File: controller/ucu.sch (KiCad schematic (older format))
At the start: 127 parts, among them J2 AMP_1, J24 AMP_4, J25 AMP_5, J26 AMP_6, J3 BUTTON, J4 AMP_2, J40 LCD, J41 TempSens1, J42 TempSens2, J47 USB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

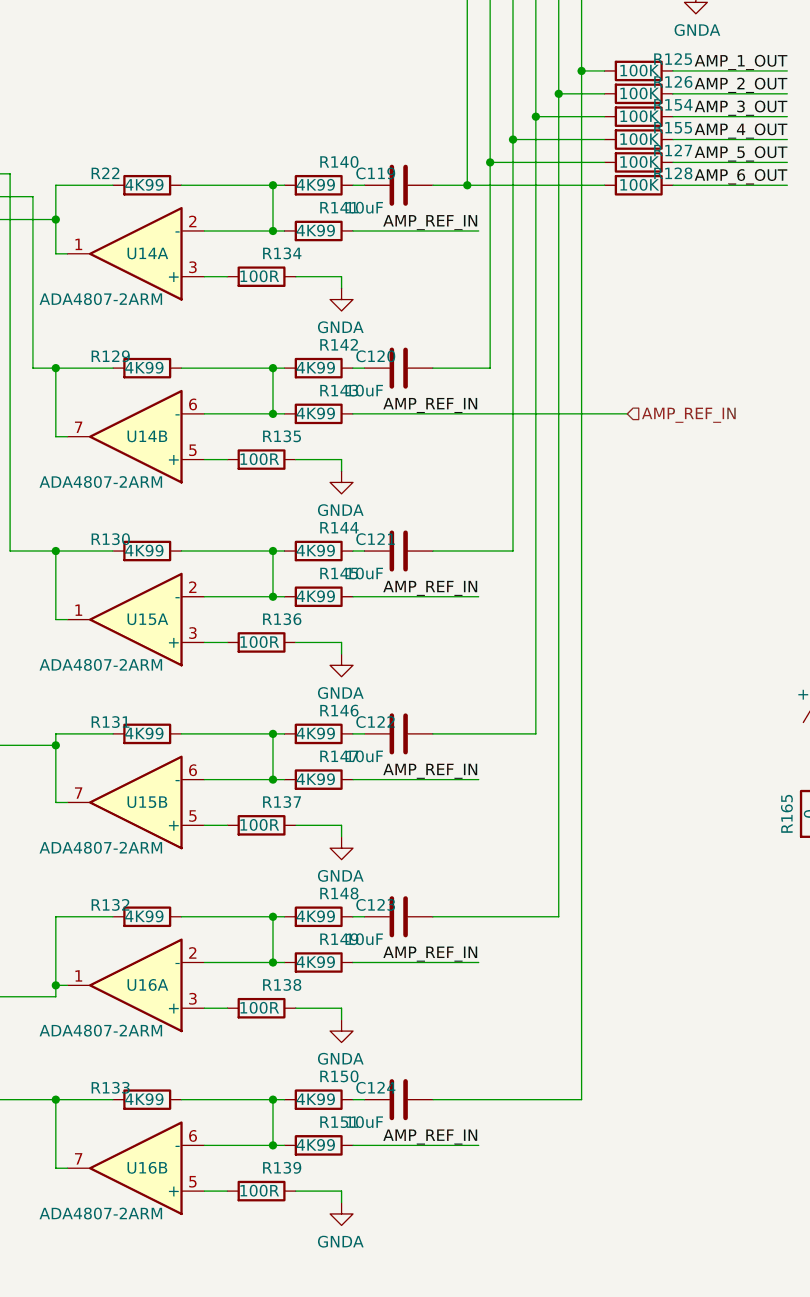
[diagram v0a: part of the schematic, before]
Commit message: update components
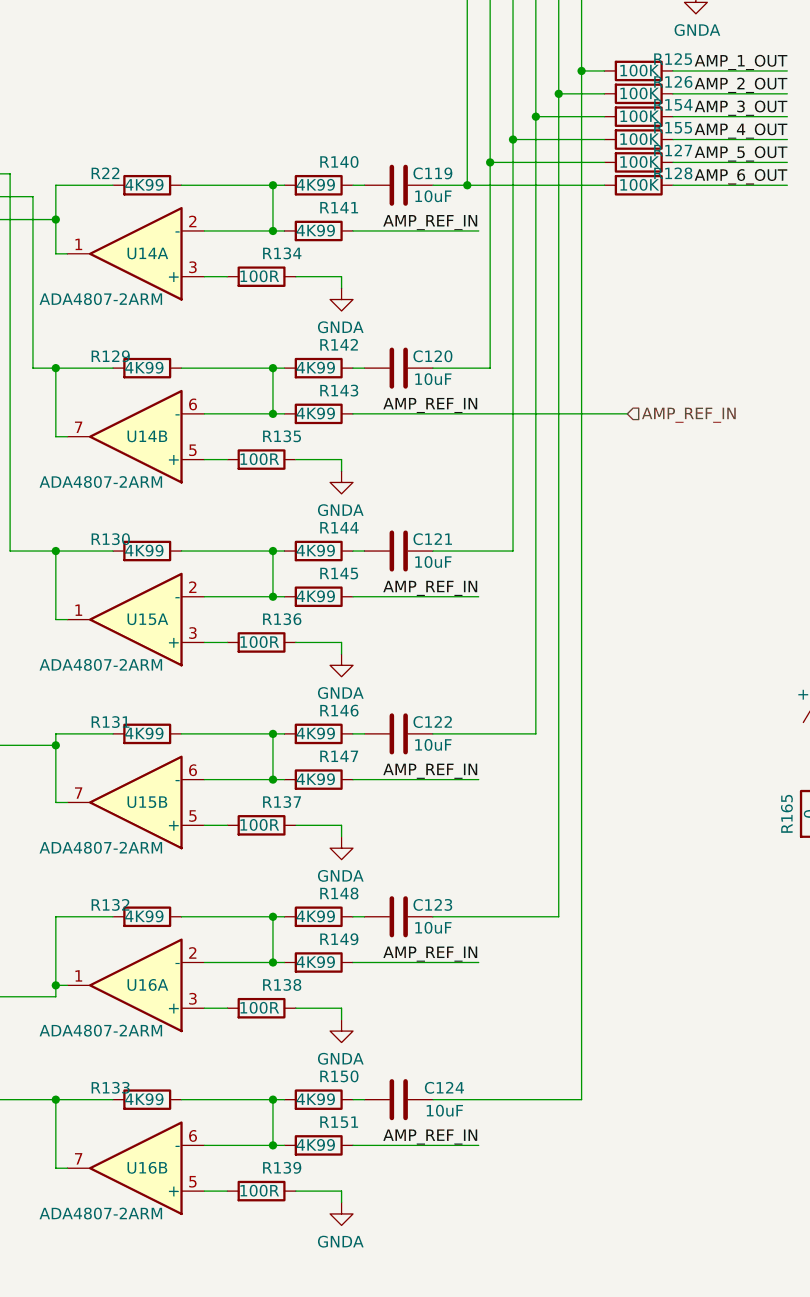
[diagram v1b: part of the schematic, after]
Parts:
- C105, C106, C114: footprint Resistor_SMD:R_0805_2012Metric_Pad1.20x1.40mm_HandSolder -> Capacitor_SMD:C_0805_2012Metric_Pad1.18x1.45mm_HandSolder
- C119, C120, C121, C122, C123, C124: footprint Capacitor_SMD:C_0603_1608Metric_Pad1.08x0.95mm_HandSolder -> Capacitor_SMD:C_0805_2012Metric_Pad1.18x1.45mm_HandSolder
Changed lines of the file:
@@
 F 0 "C106" H 2715 3846 50  0000 L CNN
 F 1 "10uF" H 2715 3755 50  0000 L CNN
-F 2 "Resistor_SMD:R_0805_2012Metric_Pad1.20x1.40mm_HandSolder" H 2638 3650 50  0001 C CNN
+F 2 "Capacitor_SMD:C_0805_2012Metric_Pad1.18x1.45mm_HandSolder" H 2638 3650 50  0001 C CNN
 F 3 "~" H 2600 3800 50  0001 C CNN
 	1    2600 3800
@@
 F 0 "C105" H 2315 3846 50  0000 L CNN
 F 1 "10uF" H 2315 3755 50  0000 L CNN
-F 2 "Resistor_SMD:R_0805_2012Metric_Pad1.20x1.40mm_HandSolder" H 2238 3650 50  0001 C CNN
+F 2 "Capacitor_SMD:C_0805_2012Metric_Pad1.18x1.45mm_HandSolder" H 2238 3650 50  0001 C CNN
 F 3 "~" H 2200 3800 50  0001 C CNN
 	1    2200 3800
@@
 F 0 "C114" H 1915 3846 50  0000 L CNN
 F 1 "10uF" H 1915 3755 50  0000 L CNN
-F 2 "Resistor_SMD:R_0805_2012Metric_Pad1.20x1.40mm_HandSolder" H 1838 3650 50  0001 C CNN
+F 2 "Capacitor_SMD:C_0805_2012Metric_Pad1.18x1.45mm_HandSolder" H 1838 3650 50  0001 C CNN
 F 3 "~" H 1800 3800 50  0001 C CNN
 	1    1800 3800
@@
 AR Path="/60CBC38F/60F38F79" Ref="C?"  Part="1"
 AR Path="/60BF25B5/60F38F79" Ref="C119"  Part="1"
-F 0 "C119" V 10150 3200 50  0000 C CNN
-F 1 "10uF" V 10300 3250 50  0000 C CNN
-F 2 "Capacitor_SMD:C_0603_1608Metric_Pad1.08x0.95mm_HandSolder" H 10238 2950 50  0001 C CNN
+F 0 "C119" V 10150 2950 50  0000 C CNN
+F 1 "10uF" V 10250 2950 50  0000 C CNN
+F 2 "Capacitor_SMD:C_0805_2012Metric_Pad1.18x1.45mm_HandSolder" H 10238 2950 50  0001 C CNN
 F 3 "~" H 10200 3100 50  0001 C CNN
 	1    10200 3100
@@
 AR Path="/60CBC38F/618385C4" Ref="C?"  Part="1"
 AR Path="/60BF25B5/618385C4" Ref="C120"  Part="1"
-F 0 "C120" V 10150 4000 50  0000 C CNN
-F 1 "10uF" V 10300 4050 50  0000 C CNN
-F 2 "Capacitor_SMD:C_0603_1608Metric_Pad1.08x0.95mm_HandSolder" H 10238 3750 50  0001 C CNN
+F 0 "C120" V 10150 3750 50  0000 C CNN
+F 1 "10uF" V 10250 3750 50  0000 C CNN
+F 2 "Capacitor_SMD:C_0805_2012Metric_Pad1.18x1.45mm_HandSolder" H 10238 3750 50  0001 C CNN
 F 3 "~" H 10200 3900 50  0001 C CNN
 	1    10200 3900
@@
 AR Path="/60CBC38F/6187A5EE" Ref="C?"  Part="1"
 AR Path="/60BF25B5/6187A5EE" Ref="C121"  Part="1"
-F 0 "C121" V 10150 4800 50  0000 C CNN
-F 1 "10uF" V 10300 4850 50  0000 C CNN
-F 2 "Capacitor_SMD:C_0603_1608Metric_Pad1.08x0.95mm_HandSolder" H 10238 4550 50  0001 C CNN
+F 0 "C121" V 10150 4550 50  0000 C CNN
+F 1 "10uF" V 10250 4550 50  0000 C CNN
+F 2 "Capacitor_SMD:C_0805_2012Metric_Pad1.18x1.45mm_HandSolder" H 10238 4550 50  0001 C CNN
 F 3 "~" H 10200 4700 50  0001 C CNN
 	1    10200 4700
@@
 AR Path="/60CBC38F/6187A62A" Ref="C?"  Part="1"
 AR Path="/60BF25B5/6187A62A" Ref="C122"  Part="1"
-F 0 "C122" V 10150 5600 50  0000 C CNN
-F 1 "10uF" V 10300 5650 50  0000 C CNN
-F 2 "Capacitor_SMD:C_0603_1608Metric_Pad1.08x0.95mm_HandSolder" H 10238 5350 50  0001 C CNN
+F 0 "C122" V 10150 5350 50  0000 C CNN
+F 1 "10uF" V 10250 5350 50  0000 C CNN
+F 2 "Capacitor_SMD:C_0805_2012Metric_Pad1.18x1.45mm_HandSolder" H 10238 5350 50  0001 C CNN
 F 3 "~" H 10200 5500 50  0001 C CNN
 	1    10200 5500
@@
 AR Path="/60CBC38F/6190D74C" Ref="C?"  Part="1"
 AR Path="/60BF25B5/6190D74C" Ref="C123"  Part="1"
-F 0 "C123" V 10150 6400 50  0000 C CNN
-F 1 "10uF" V 10300 6450 50  0000 C CNN
-F 2 "Capacitor_SMD:C_0603_1608Metric_Pad1.08x0.95mm_HandSolder" H 10238 6150 50  0001 C CNN
+F 0 "C123" V 10150 6150 50  0000 C CNN
+F 1 "10uF" V 10250 6150 50  0000 C CNN
+F 2 "Capacitor_SMD:C_0805_2012Metric_Pad1.18x1.45mm_HandSolder" H 10238 6150 50  0001 C CNN
 F 3 "~" H 10200 6300 50  0001 C CNN
 	1    10200 6300
@@
 AR Path="/60CBC38F/6190D788" Ref="C?"  Part="1"
 AR Path="/60BF25B5/6190D788" Ref="C124"  Part="1"
-F 0 "C124" V 10150 7200 50  0000 C CNN
-F 1 "10uF" V 10300 7250 50  0000 C CNN
-F 2 "Capacitor_SMD:C_0603_1608Metric_Pad1.08x0.95mm_HandSolder" H 10238 6950 50  0001 C CNN
+F 0 "C124" V 10150 6900 50  0000 C CNN
+F 1 "10uF" V 10250 6900 50  0000 C CNN
+F 2 "Capacitor_SMD:C_0805_2012Metric_Pad1.18x1.45mm_HandSolder" H 10238 6950 50  0001 C CNN
 F 3 "~" H 10200 7100 50  0001 C CNN
 	1    10200 7100

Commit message: Fix misc issues
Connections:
- net PON: now also U4.84 (PD3)
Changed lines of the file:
@@
 Wire Wire Line
 	14150 3650 14800 3650
+Text Label 2250 6650 0    50   ~ 0
+PON
+Wire Wire Line
+	2250 6650 2750 6650
 $EndSCHEMATC
